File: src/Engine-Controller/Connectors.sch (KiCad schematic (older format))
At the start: 7 parts, among them P3 SBH11-PBPC-D05-RA-BK, P4 0901471110, P5 66953-005LF, P7 0901471110, U4 SN74LV07ADR

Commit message: Fixed Schematic ERC erros
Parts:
- removed None02, None07: 3.3V, symbol Engine-Controller:3.3V
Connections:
- no-connect marks 0 -> 2
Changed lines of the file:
@@
 	7800 2650 7800 2900
-$Comp
-L Engine-Controller:3.3V None02
-U 1 1 61392439
-P 7800 1500
-F 0 "None02" H 7928 1489 50  0001 L CNN
-F 1 "3.3V" H 7726 1601 50  0000 L CNN
-F 2 "" H 7800 1500 50  0001 C CNN
-F 3 "" H 7800 1500 50  0001 C CNN
-	1    7800 1500
-	1    0    0    -1
-$EndComp
 $Comp
 L Engine-Controller:SN74LV07ADR U4
@@
 	1    0    0    -1
 $EndComp
-Wire Wire Line
-	7800 1750 7800 1650
 Wire Notes Line
 	5200 1100 10300 1100
@@
 Wire Wire Line
 	2000 5350 2000 5500
-$Comp
-L Engine-Controller:3.3V None07
-U 1 1 61C0A50F
-P 1850 4200
-F 0 "None07" H 1978 4189 50  0001 L CNN
-F 1 "3.3V" H 1771 4292 50  0000 L CNN
-F 2 "" H 1850 4200 50  0001 C CNN
-F 3 "" H 1850 4200 50  0001 C CNN
-	1    1850 4200
-	1    0    0    -1
-$EndComp
 Wire Wire Line
 	2000 5250 1850 5250
 Wire Wire Line
-	1850 5250 1850 4350
+	1850 5250 1850 4300
 Wire Notes Line
 	6900 5800 3900 5800
@@
 Text Notes 1450 3850 0    50   ~ 0
 Analog-to-Digital Converter\n
+Text GLabel 7800 1500 1    50   Input ~ 0
+3.3V
+Wire Wire Line
+	7800 1500 7800 1750
+Text GLabel 1850 4300 1    50   Input ~ 0
+3.3V
+NoConn ~ 5150 4600
+NoConn ~ 5150 4800
 $EndSCHEMATC

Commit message: Routed decoupling caps
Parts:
- P3: footprint 66953-005LF_AMP -> Engine-Controller:SBH11-PBPC-D05-RA-BK
- P4, P7: footprint 66953-005LF_AMP -> Engine-Controller:0901471110
- P5: footprint 66953-005LF_AMP -> Engine-Controller:66953-005LF
- U4: footprint SOIC127P600X175-14N -> Engine-Controller:SN74LV07ADR
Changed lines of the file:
@@
 F 0 "P4" H 9428 1553 60  0000 L CNN
 F 1 "0901471110" H 9428 1447 60  0000 L CNN
-F 2 "66953-005LF_AMP" H 9050 750 60  0001 C CNN
+F 2 "Engine-Controller:0901471110" H 9050 750 60  0001 C CNN
 F 3 "" H 8900 1950 60  0001 C CNN
 	1    8900 1950
@@
 F 0 "P5" H 9578 4003 60  0000 L CNN
 F 1 "66953-005LF" H 9578 3897 60  0000 L CNN
-F 2 "66953-005LF_AMP" H 9200 3200 60  0001 C CNN
+F 2 "Engine-Controller:66953-005LF" H 9200 3200 60  0001 C CNN
 F 3 "" H 9050 4400 60  0001 C CNN
 	1    9050 4400
@@
 F 0 "U4" H 7100 3020 50  0000 C CNN
 F 1 "SN74LV07ADR" H 7100 2929 50  0000 C CNN
-F 2 "SOIC127P600X175-14N" H 6650 1350 50  0001 L BNN
+F 2 "Engine-Controller:SN74LV07ADR" H 6650 1350 50  0001 L BNN
 F 3 "" H 7100 2250 50  0001 L BNN
 	1    7100 2250
@@
 F 0 "P3" H 5392 4687 60  0000 C CNN
 F 1 "SBH11-PBPC-D05-RA-BK" H 5392 4581 60  0000 C CNN
-F 2 "66953-005LF_AMP" H 5300 3200 60  0001 C CNN
+F 2 "Engine-Controller:SBH11-PBPC-D05-RA-BK" H 5300 3200 60  0001 C CNN
 F 3 "" H 5150 4400 60  0001 C CNN
 	1    5150 4400
@@
 F 0 "P7" H 2528 4053 60  0000 L CNN
 F 1 "0901471110" H 2528 3947 60  0000 L CNN
-F 2 "66953-005LF_AMP" H 2150 3250 60  0001 C CNN
+F 2 "Engine-Controller:0901471110" H 2150 3250 60  0001 C CNN
 F 3 "" H 2000 4450 60  0001 C CNN
 	1    2000 4450

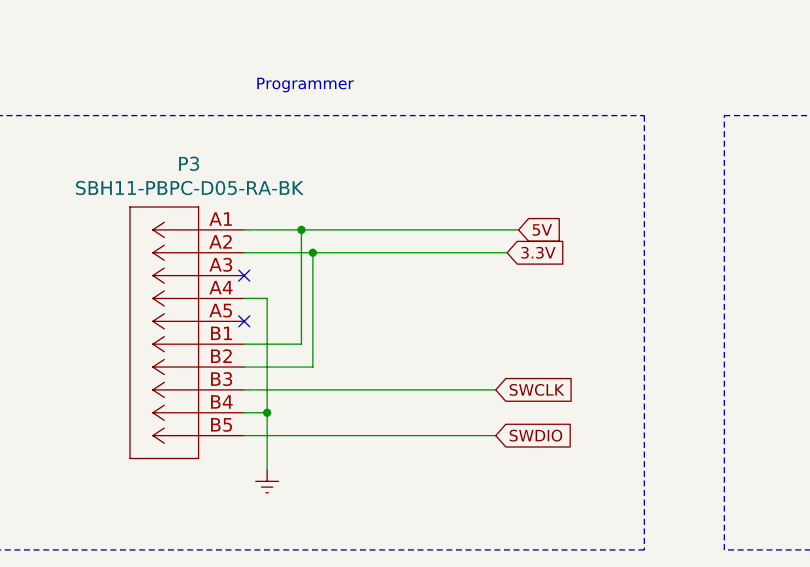
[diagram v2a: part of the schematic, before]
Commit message: Resolved DRC issues
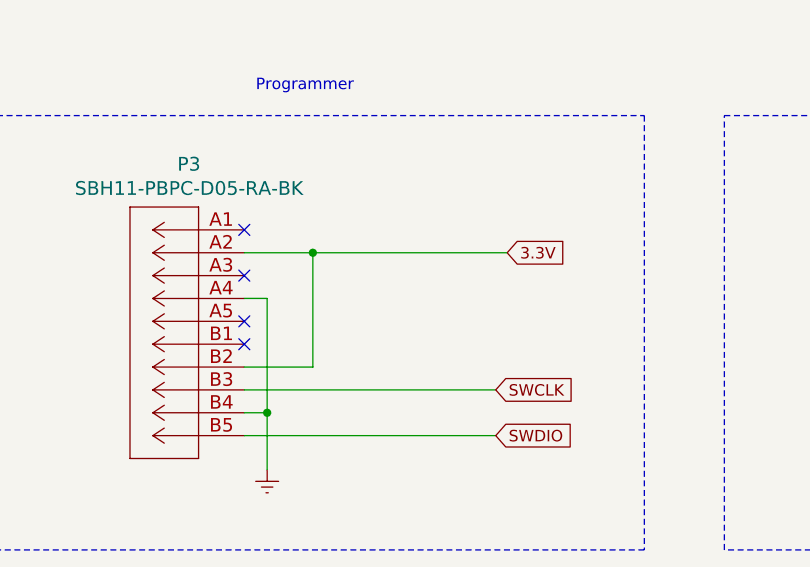
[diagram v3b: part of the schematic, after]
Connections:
- net 5V: no longer names the net of P3.A1
- net 5V: no longer P3.B1
- no-connect marks 2 -> 4
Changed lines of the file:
@@
 Text GLabel 6300 4500 2    50   Input ~ 0
 3.3V
-Text GLabel 6350 4400 2    50   Input ~ 0
-5V
 $Comp
 L power:Earth #PWR?
@@
 	-1   0    0    -1
 $EndComp
-Wire Wire Line
-	5150 4400 5400 4400
-Wire Wire Line
-	5150 4900 5400 4900
-Wire Wire Line
-	5400 4900 5400 4400
-Connection ~ 5400 4400
-Wire Wire Line
-	5400 4400 6350 4400
 Wire Wire Line
 	5150 4700 5250 4700
@@
 NoConn ~ 5150 4600
 NoConn ~ 5150 4800
+NoConn ~ 5150 4900
+NoConn ~ 5150 4400
 $EndSCHEMATC

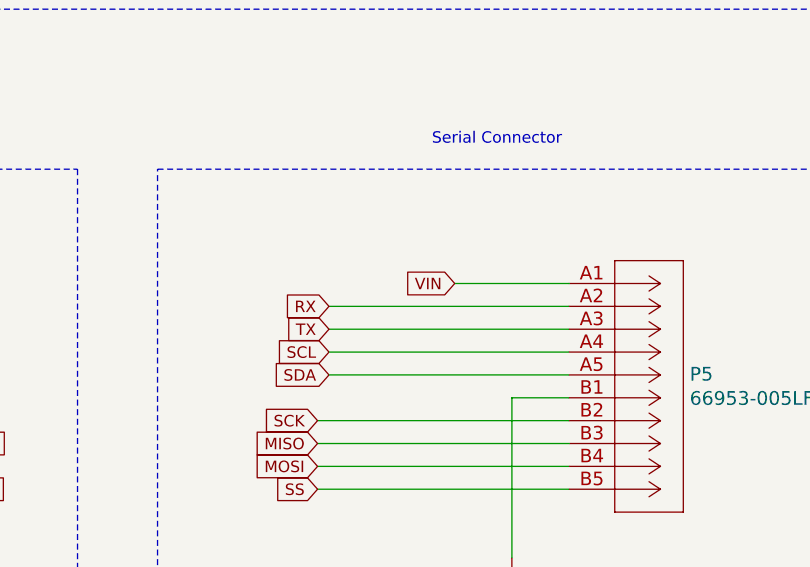
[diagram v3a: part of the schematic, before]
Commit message: Added voltage source selector to schematic
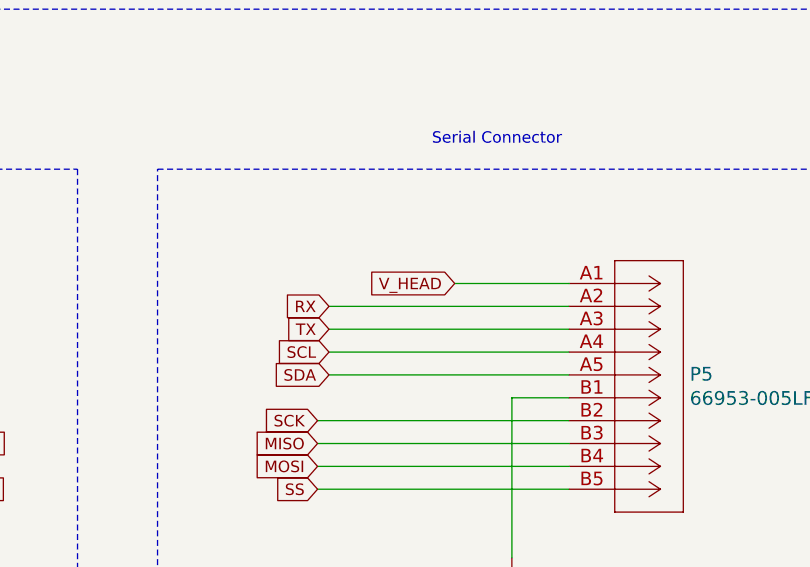
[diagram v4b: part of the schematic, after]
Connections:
- net VIN renamed V_HEAD
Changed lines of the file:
@@
 	1    0    0    -1
 $EndComp
-Text GLabel 8550 4400 0    50   Input ~ 0
-VIN
 Wire Notes Line
 	10400 3900 10400 5800
@@
 NoConn ~ 5150 4900
 NoConn ~ 5150 4400
+Text GLabel 8550 4400 0    50   Input ~ 0
+V_HEAD
 $EndSCHEMATC

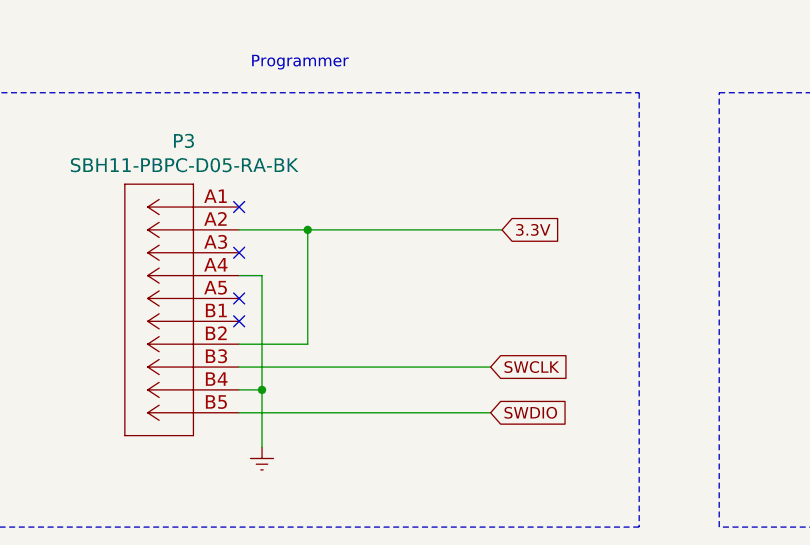
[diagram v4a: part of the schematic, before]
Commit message: Removed SWD 3.3V connections
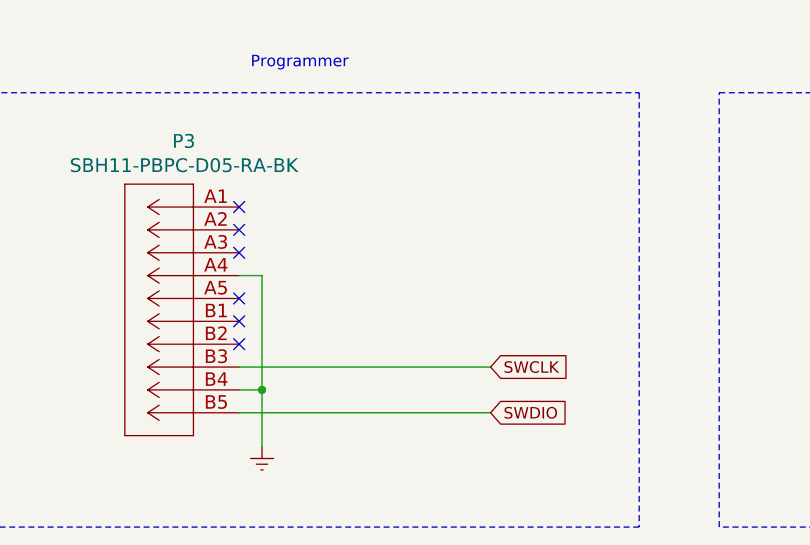
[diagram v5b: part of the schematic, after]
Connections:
- net 3.3V: no longer P3.A2, P3.B2
- no-connect marks 4 -> 6
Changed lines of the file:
@@
 Text GLabel 6250 5300 2    50   Input ~ 0
 SWDIO
-Text GLabel 6300 4500 2    50   Input ~ 0
-3.3V
 $Comp
 L power:Earth #PWR?
@@
 Wire Wire Line
 	5250 5200 5250 5450
-Wire Wire Line
-	6300 4500 5450 4500
-Wire Wire Line
-	5150 5000 5450 5000
-Wire Wire Line
-	5450 5000 5450 4500
-Connection ~ 5450 4500
-Wire Wire Line
-	5450 4500 5150 4500
 Wire Wire Line
 	6250 5300 5150 5300
@@
 Text GLabel 8550 4400 0    50   Input ~ 0
 V_HEAD
+NoConn ~ 5150 4500
+NoConn ~ 5150 5000
 $EndSCHEMATC

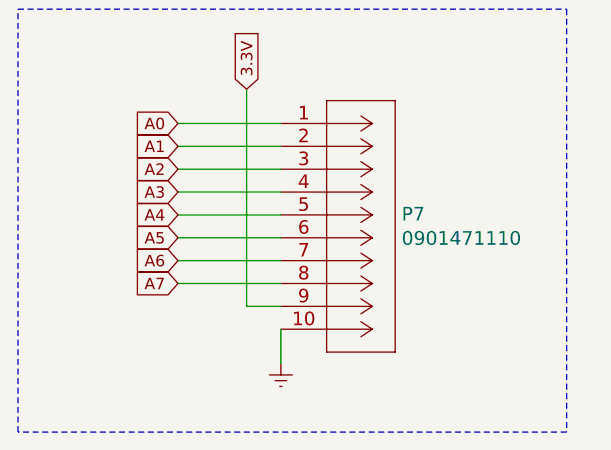
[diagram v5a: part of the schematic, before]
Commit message: Changed MCU from M4 to M7
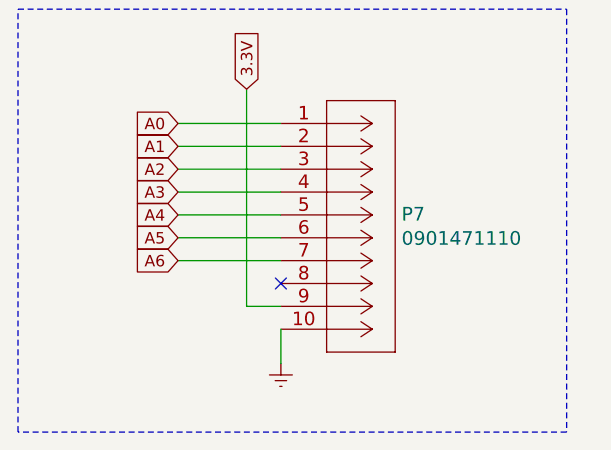
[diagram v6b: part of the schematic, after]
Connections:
- net A7: no longer names the net of P7.8
- no-connect marks 6 -> 7
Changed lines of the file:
@@
 Text GLabel 1550 5050 0    50   Input ~ 0
 A6
-Text GLabel 1550 5150 0    50   Input ~ 0
-A7
 Wire Wire Line
 	1550 4550 2000 4550
@@
 Wire Wire Line
 	1550 5050 2000 5050
-Wire Wire Line
-	1550 5150 2000 5150
 $Comp
 L power:Earth #PWR07
@@
 NoConn ~ 5150 4500
 NoConn ~ 5150 5000
+NoConn ~ 2000 5150
 $EndSCHEMATC
